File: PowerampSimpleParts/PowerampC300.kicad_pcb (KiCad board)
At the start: 2 copper layers, 219 x 63 mm, 121 parts, among them J1 Conn_01x02, J2 Conn_01x02, J3 Conn_01x02, J4 Conn_01x01, J5 Conn_01x01, J6 Conn_01x01, J7 Conn_01x01, J8 Conn_01x02, J9 Conn_Coaxial, Q1 2N5551, Q10 2N5401, Q11 TIP41C, Q12 2N5551, Q13 2N5551, Q14 2N5401, Q15 TIP41C, Q16 TIP42C, Q17 TIP41C, Q18 TIP42C, Q19 TIP41C, Q2 2N5551, Q20 TIP42C, Q21 TIP41C, Q22 TIP42C, Q23 TIP41C, Q24 TIP42C, Q25 2N5551, Q26 2N5401, Q3 2N5401, Q4 2N5401, Q5 2N5551, Q6 2N5551, Q7 2N5551, Q8 2N5401, Q9 2N5401

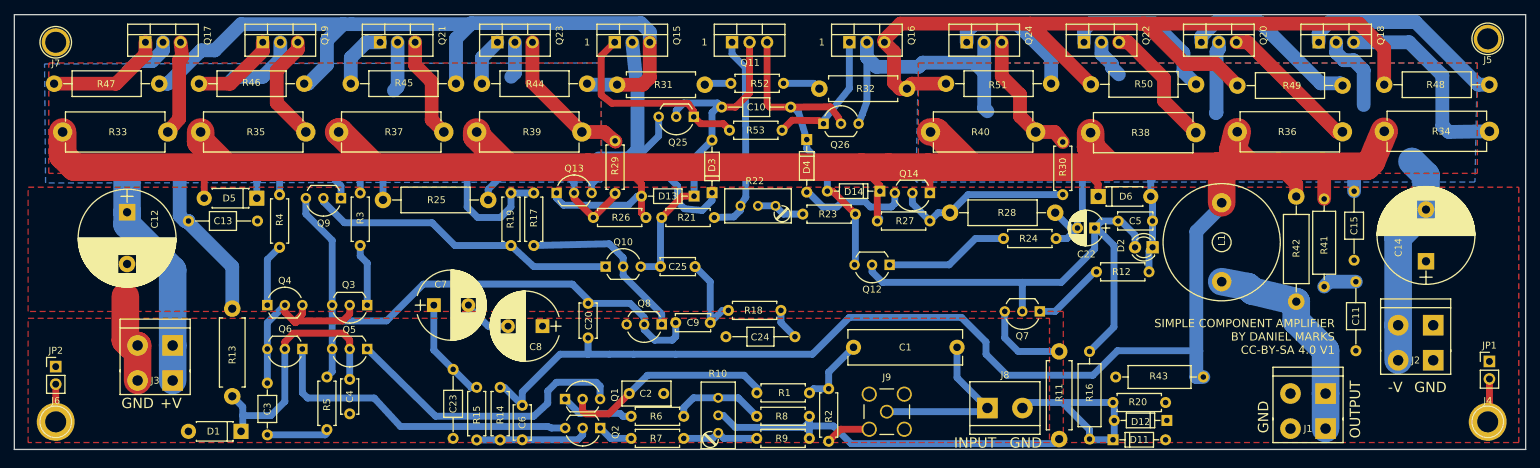
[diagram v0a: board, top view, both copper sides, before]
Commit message: Minor tweaks to PowerampSimpleParts
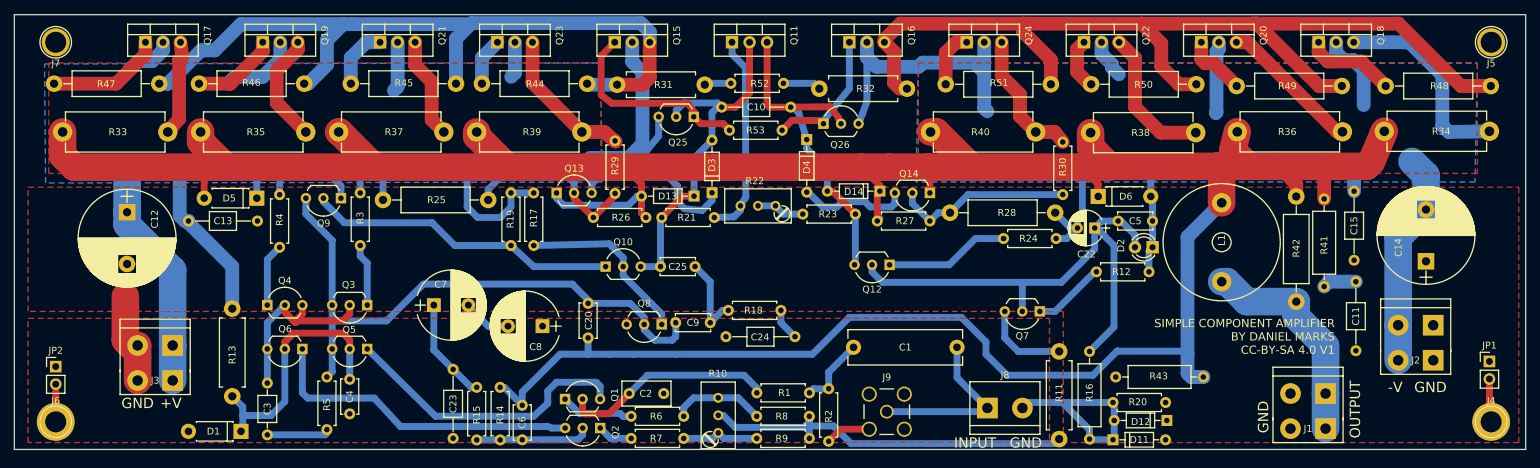
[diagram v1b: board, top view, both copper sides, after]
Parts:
- moved R48 15.5 mm to (251.0, 53.3), turned to 180 degrees
- moved R50 15.3 mm to (208.3, 53.1), turned to 180 degrees
- moved R51 15.2 mm to (187.2, 53.1), turned to 180 degrees
- moved R49 15.1 mm to (229.4, 53.3), turned to 180 degrees
- moved J5 0.71 mm to (251.0, 47.0)
- moved J4 0.50 mm to (251.0, 102.0)
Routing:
- net Net-(Q18-Pad1): track 30.5 -> 13.2 mm
- net Net-(Q20-Pad1): track 26.0 -> 9.21 mm
- net Net-(Q22-Pad1): track 23.7 -> 7.49 mm
- net Net-(Q16-Pad3): track 125.2 -> 141.3 mm
- net Net-(Q24-Pad1): track 19.9 -> 8.24 mm
- net Net-(Q22-Pad3): track 18.5 -> 20.7 mm
- net Net-(C20-Pad2): track 457.2 -> 459.2 mm
- net OUTPUT: track 31.5 -> 32.2 mm
- net +40V: track 157.9 -> 158.5 mm
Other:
- board text removed: "1"

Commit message: A few minor tweaks to PowerampSimpleParts layout
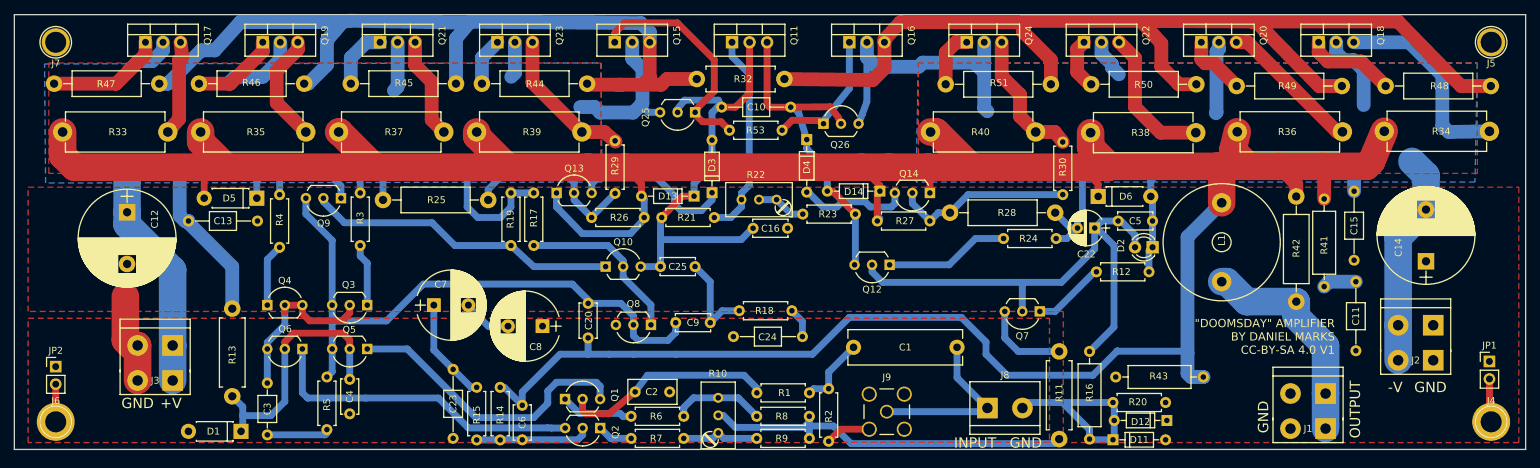
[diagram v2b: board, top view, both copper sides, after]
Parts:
- removed R31: 33R, Resistors_THT:R_Axial_DIN0411_L9.9mm_D3.6mm_P12.70mm_Horizontal
- removed R52: 100R, Resistors_THT:R_Axial_DIN0207_L6.3mm_D2.5mm_P7.62mm_Horizontal
- added C16: NC, Capacitors_THT:C_Disc_D5.0mm_W2.5mm_P5.00mm, F.Cu at (149.1, 74.0)
- D1: value 1N4752A -> 1N4749A
- moved R32 17.8 mm to (148.6, 52.3)
- moved R18 1.59 mm to (142.1, 85.9)
- moved Q8 1.56 mm to (129.2, 88.0)
- moved C24 1.09 mm to (151.2, 89.7)
- moved R22 0.91 mm to (147.4, 69.8)
- moved C2 0.89 mm to (132.0, 97.7)
- moved Q25 0.68 mm to (135.7, 57.1)
- moved R26 0.25 mm to (120.7, 72.4)
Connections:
- R32 pad 2: Net-(R32-Pad2) -> Net-(Q15-Pad3)
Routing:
- net BIAS1: track 51.9 -> 66.1 mm
- net +40V: track 158.5 -> 144.3 mm
- net Net-(Q16-Pad3): track 141.3 -> 153.9 mm
- net Net-(Q15-Pad3): track 112.0 -> 121.5 mm
- net Net-(R32-Pad2): track 5.52 -> 0.00 mm
- net Net-(R31-Pad1): track 3.86 -> 0.00 mm
- net Net-(Q15-Pad1): track 30.1 -> 33.6 mm
- net Net-(C20-Pad2): track 459.2 -> 462.6 mm
- net Net-(C3-Pad2): track 28.7 -> 26.0 mm
- net Net-(C25-Pad1): track 12.4 -> 14.0 mm
- net Net-(Q11-Pad1): track 29.6 -> 30.6 mm
- net Net-(Q10-Pad2): track 25.8 -> 24.8 mm
- net Net-(D3-Pad1): track 24.1 -> 23.5 mm
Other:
- board text added: ""DOOMSDAY" AMPLIFIER BY DANIEL MARKS CC-BY-SA 4.0 V1"
- board text removed: "SIMPLE COMPONENT AMPLIFIER BY DANIEL MARKS CC-BY-SA 4.0 V1"

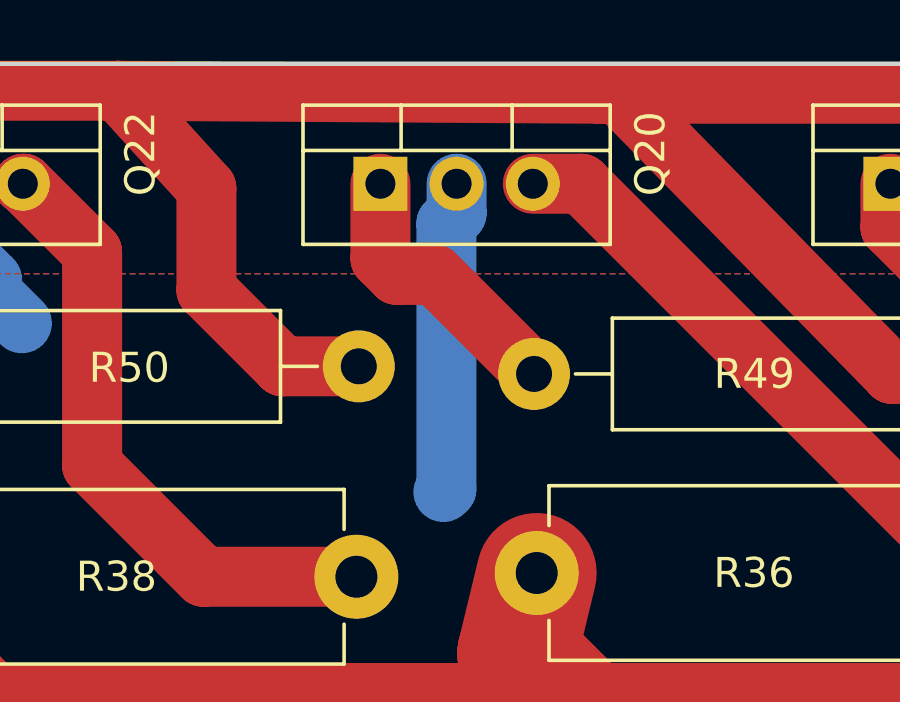
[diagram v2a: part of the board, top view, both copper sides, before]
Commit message: Fixed some silkscreening
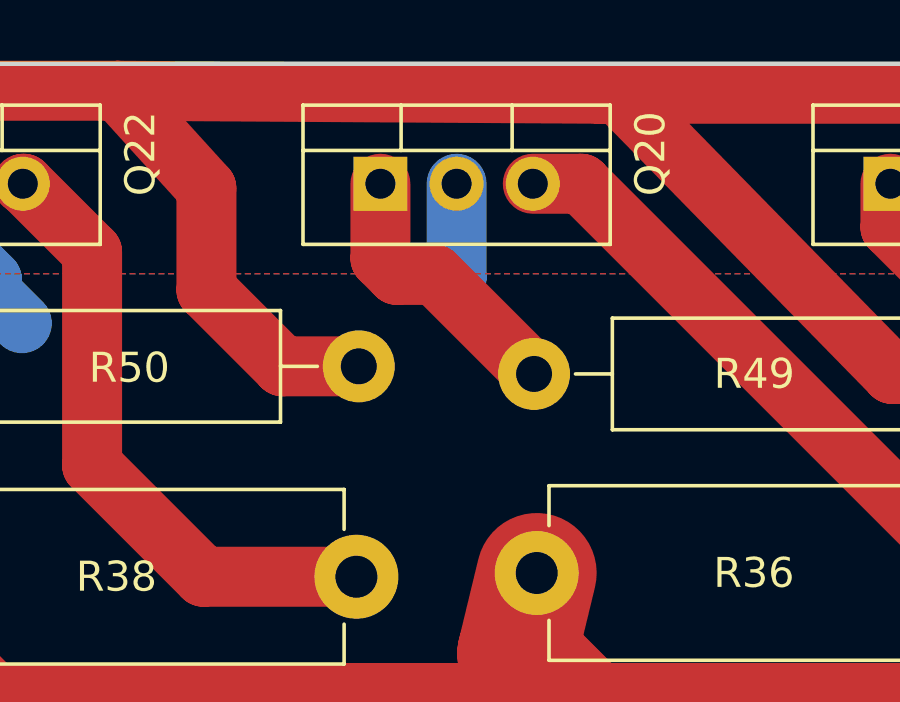
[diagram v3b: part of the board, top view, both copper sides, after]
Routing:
- net -40V: track 135.3 -> 128.2 mm
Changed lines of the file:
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@@
     (thickness 1.6)
     (drawings 13)
-    (tracks 621)
+    (tracks 619)
     (zones 0)
     (modules 120)
@@
   (segment (start 138.9 56.4) (end 138.1 57.2) (width 1) (layer B.Cu) (net 58))
   (segment (start 138.1 57.2) (end 138.1 61.18) (width 1) (layer B.Cu) (net 58) (status 20))
+  (segment (start 211.54 47) (end 211.54 50.12) (width 2) (layer B.Cu) (net 59) (status 400000))
+  (segment (start 211.54 50.12) (end 211.33 50.33) (width 2) (layer B.Cu) (net 59))
   (segment (start 201.422 80.264) (end 201.422 77.216) (width 1) (layer B.Cu) (net 59))
   (segment (start 201.422 77.216) (end 201.93 76.708) (width 1) (layer B.Cu) (net 59))
@@
   (segment (start 229.65 49.6) (end 231.075 49.6) (width 2) (layer B.Cu) (net 59))
   (segment (start 228.54 48.49) (end 229.65 49.6) (width 2) (layer B.Cu) (net 59))
-  (segment (start 211.54 47) (end 211.54 47.985) (width 2) (layer B.Cu) (net 59))
-  (segment (start 211.2 57.175) (end 211.1 57.275) (width 2) (layer B.Cu) (net 59))
-  (segment (start 211.2 48.325) (end 211.2 57.175) (width 2) (layer B.Cu) (net 59))
-  (segment (start 211.54 47.985) (end 211.2 48.325) (width 2) (layer B.Cu) (net 59))
   (segment (start 194.54 47) (end 194.54 48.69) (width 2) (layer B.Cu) (net 59))
   (segment (start 196.05 50.65) (end 197.05 51.65) (width 2) (layer B.Cu) (net 59))

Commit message: Updated gerbers
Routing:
- net BIAS1: track 66.1 -> 67.0 mm
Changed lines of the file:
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@@
   )
   (setup
-    (last_trace_width 2)
+    (last_trace_width 0.25)
     (user_trace_width 0.5)
     (user_trace_width 1)
@@
   (segment (start 133.78 69.3) (end 130.81 72.39) (width 1) (layer F.Cu) (net 58) (status 20))
   (segment (start 133.11 57.15) (end 132.91 56.89) (width 1) (layer B.Cu) (net 58) (status 10))
-  (segment (start 139.02 55.39) (end 139.5 56.4) (width 1) (layer B.Cu) (net 58))
-  (segment (start 134.12 55.39) (end 139.02 55.39) (width 1) (layer B.Cu) (net 58))
-  (segment (start 132.91 56.89) (end 134.12 55.39) (width 1) (layer B.Cu) (net 58))
+  (segment (start 139.02 54.882) (end 139.5 56.4) (width 1) (layer B.Cu) (net 58))
+  (segment (start 134.12 54.882) (end 139.02 54.882) (width 1) (layer B.Cu) (net 58))
+  (segment (start 132.91 56.89) (end 134.12 54.882) (width 1) (layer B.Cu) (net 58))
   (segment (start 143.54 47) (end 143.54 54.36) (width 1) (layer F.Cu) (net 58))
   (segment (start 141.5 56.4) (end 139.5 56.4) (width 1) (layer F.Cu) (net 58))
@@
   (segment (start 138.9 56.4) (end 138.1 57.2) (width 1) (layer B.Cu) (net 58))
   (segment (start 138.1 57.2) (end 138.1 61.18) (width 1) (layer B.Cu) (net 58) (status 20))
-  (segment (start 211.54 47) (end 211.54 50.12) (width 2) (layer B.Cu) (net 59) (status 400000))
+  (segment (start 211.54 47) (end 211.54 50.12) (width 2) (layer B.Cu) (net 59))
   (segment (start 211.54 50.12) (end 211.33 50.33) (width 2) (layer B.Cu) (net 59))
   (segment (start 201.422 80.264) (end 201.422 77.216) (width 1) (layer B.Cu) (net 59))
